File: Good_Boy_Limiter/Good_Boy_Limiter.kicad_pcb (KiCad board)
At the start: 2 copper layers, 36 parts, among them Q2 AO3422, SW3 RESET1, SW4 BOOT1, U1 ESP32-S3-WROOM-1, U2 TC4427EOA_C636891, U3 LM2576HVR-12, U4 LM2576SX-3.3/NOPB, U5 MAX40200AUK+T, U6 AMS1117-3.3, U7 MAX40200AUK+T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

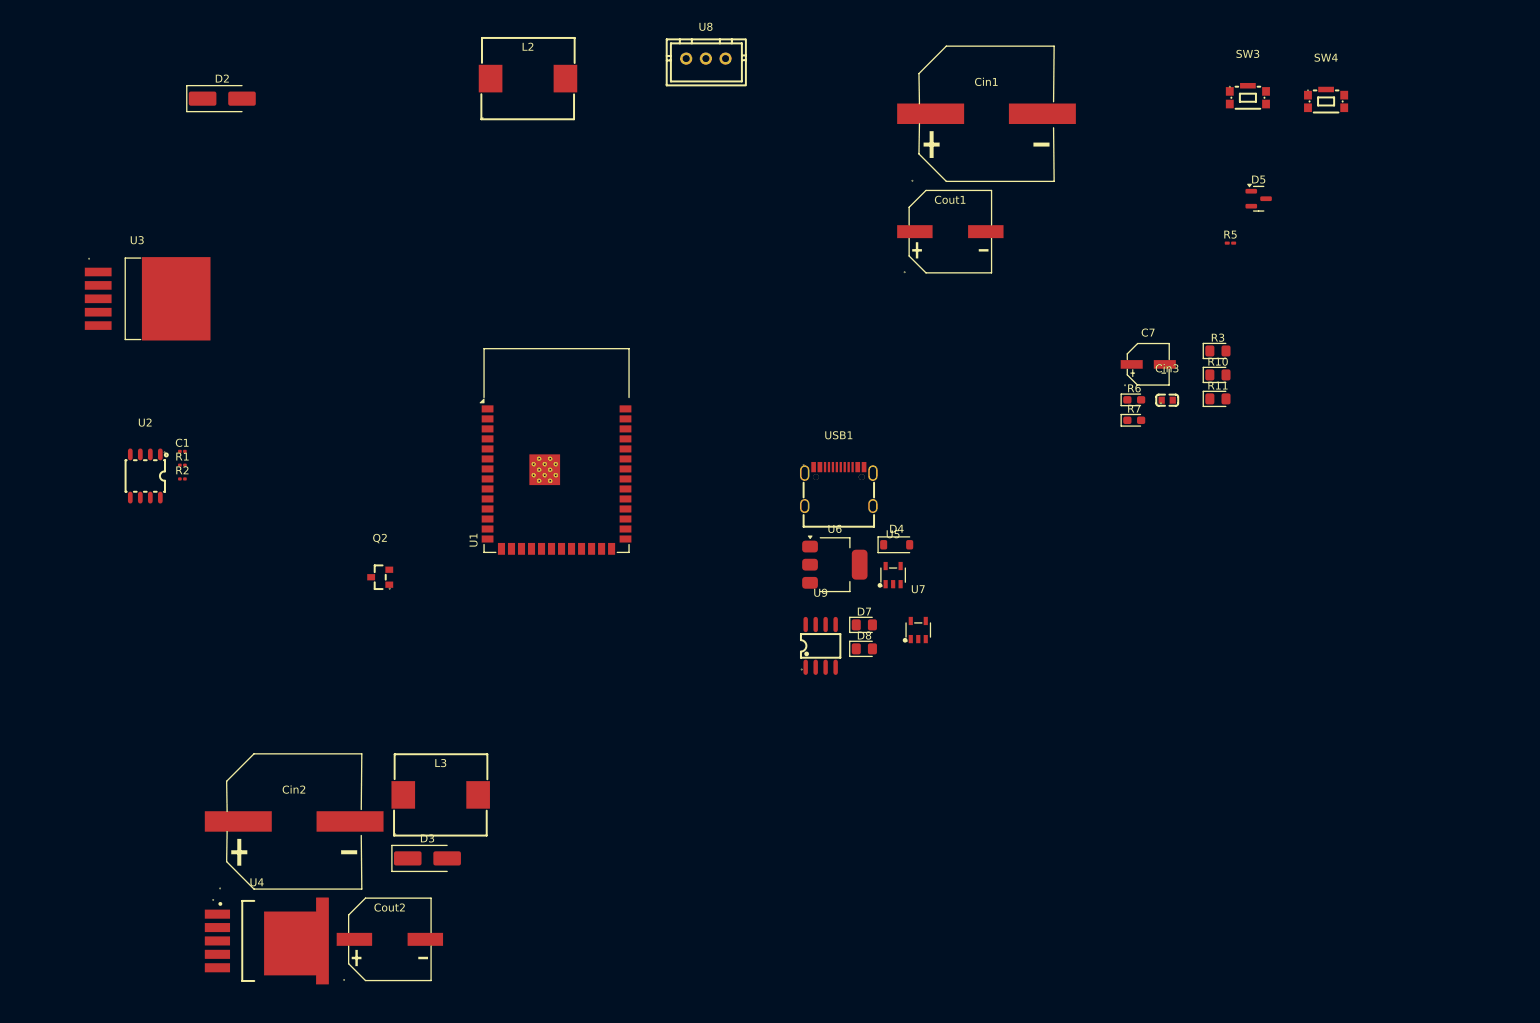
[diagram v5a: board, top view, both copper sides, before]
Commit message: Added all footprints
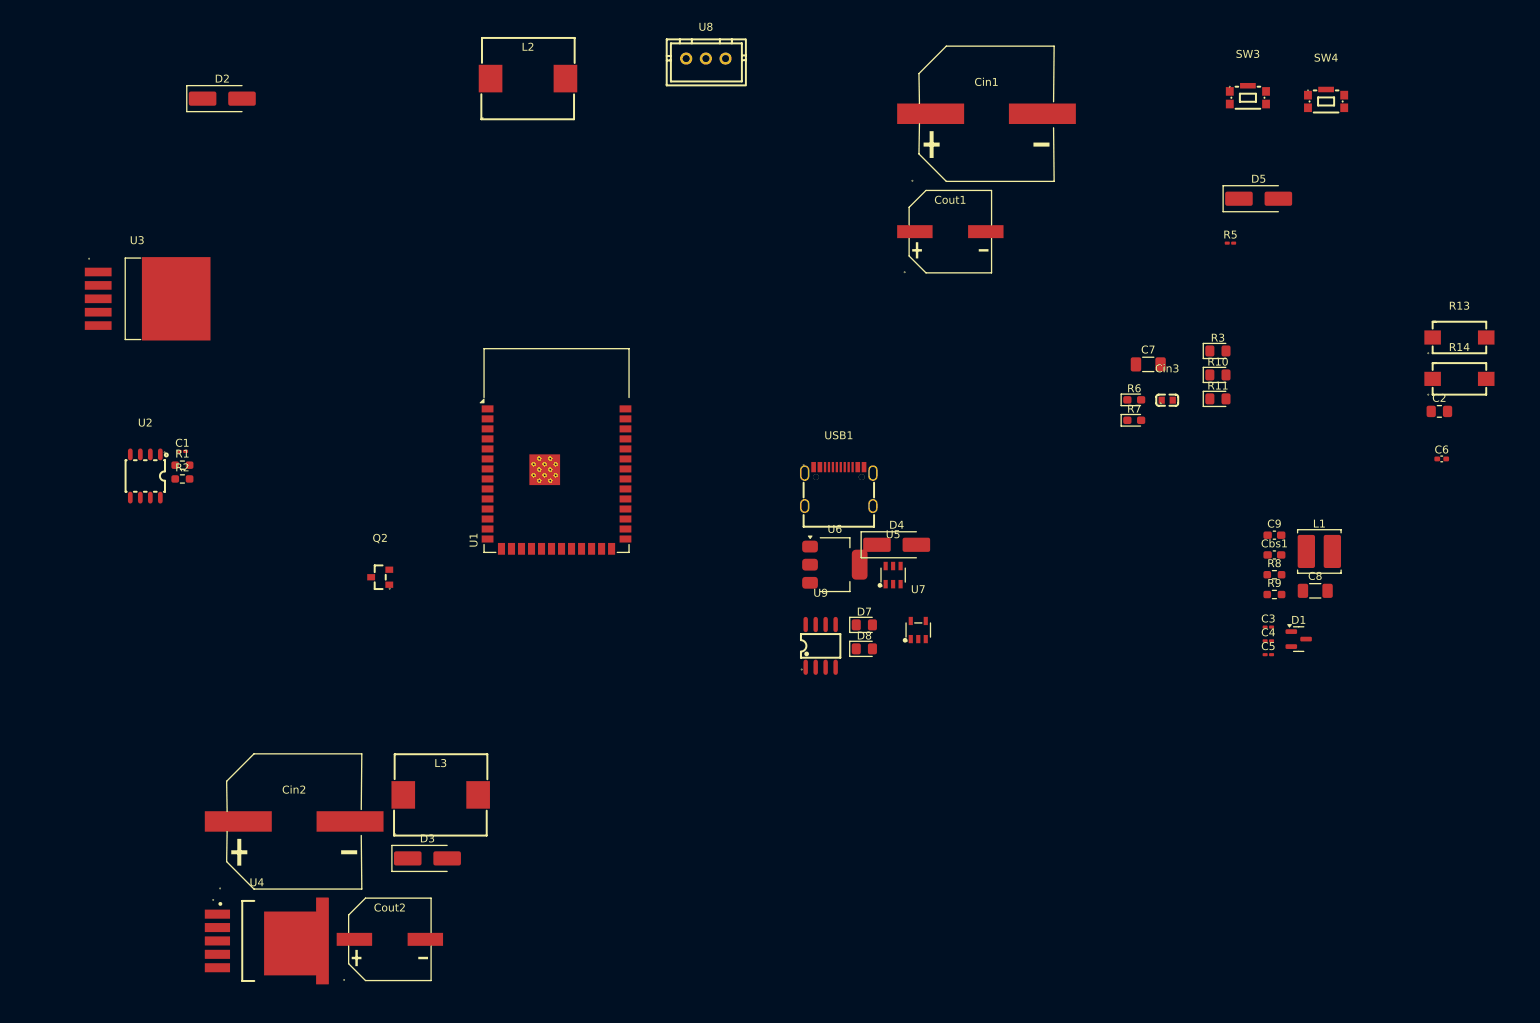
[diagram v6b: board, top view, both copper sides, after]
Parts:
- added C2: 1uF, Capacitor_SMD:C_0805_2012Metric_Pad1.18x1.45mm_HandSolder, F.Cu at (202.3, 70.2)
- added C3: 100nF, Capacitor_SMD:C_0201_0603Metric_Pad0.64x0.40mm_HandSolder, F.Cu at (180.6, 97.5)
- added C4: 10uF, Capacitor_SMD:C_0201_0603Metric_Pad0.64x0.40mm_HandSolder, F.Cu at (180.6, 99.3)
- added C5: 100nF, Capacitor_SMD:C_0201_0603Metric_Pad0.64x0.40mm_HandSolder, F.Cu at (180.6, 101.0)
- added C6: 100nF, Capacitor_SMD:C_0402_1005Metric_Pad0.74x0.62mm_HandSolder, F.Cu at (202.6, 76.2)
- added C8: 22uF, Capacitor_SMD:C_1206_3216Metric_Pad1.33x1.80mm_HandSolder, F.Cu at (186.6, 92.9)
- added C9: 100nF, Capacitor_SMD:C_0603_1608Metric_Pad1.08x0.95mm_HandSolder, F.Cu at (181.4, 85.9)
- added Cbs1: 10nF, Capacitor_SMD:C_0603_1608Metric_Pad1.08x0.95mm_HandSolder, F.Cu at (181.4, 88.4)
- added D1: 3V3, Package_TO_SOT_SMD:SOT-23, F.Cu at (184.5, 99.1)
- added L1: 10uH, Inductor_SMD:L_Cenker_CKCS5040, F.Cu at (187.1, 87.9)
- added R13: 100, easyeda2kicad:RES-SMD_L6.7-W4.0-LS7.9, F.Cu at (204.9, 60.8)
- added R14: 100, easyeda2kicad:RES-SMD_L6.7-W4.0-LS7.9, F.Cu at (204.9, 66.0)
- added R8: 100k, Resistor_SMD:R_0603_1608Metric_Pad0.98x0.95mm_HandSolder, F.Cu at (181.4, 90.9)
- added R9: 22k, Resistor_SMD:R_0603_1608Metric_Pad0.98x0.95mm_HandSolder, F.Cu at (181.4, 93.4)
- C1: footprint Capacitor_SMD:C_0201_0603Metric -> Capacitor_SMD:C_0201_0603Metric_Pad0.64x0.40mm_HandSolder
- C7: footprint easyeda2kicad:CAP-SMD_BD5.0-L5.3-W5.3-FD -> Capacitor_SMD:C_1206_3216Metric_Pad1.33x1.80mm_HandSolder
- D4: value 1N4148W -> SS34; footprint Diode_SMD:D_SOD-123 -> Diode_SMD:D_SMA_Handsoldering
- D5: value 3V3 -> SS34; footprint Package_TO_SOT_SMD:SOT-23 -> Diode_SMD:D_SMA_Handsoldering
- R1, R2: footprint Resistor_SMD:R_0201_0603Metric -> Resistor_SMD:R_0603_1608Metric_Pad0.98x0.95mm_HandSolder
- U5: value MAX40200AUK+T -> SY8120B; footprint easyeda2kicad:TSOT-23-5_L2.9-W1.6-P0.95-LS2.8-BL -> easyeda2kicad:SOT-23-6_L2.9-W1.6-P0.95-LS2.8-BL
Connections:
- C7 pad 1: Net-(C7-Pad1) -> /3V3
- D4 pad 1: /USB Communication/+5VUSB -> /3V3 Selector/Vin
- D4 pad 2: /3V3LDO -> /5VUSB
- D5 pad 1: GND -> /3V3 Selector/Vin
- D5 pad 2: unconnected-(D5-NC-Pad2) -> /+12V
- U5 pad 1: /3V3LDO -> Net-(U5-BS)
- U5 pad 3: /3V3LDO -> Net-(U5-FB)
- U5 pad 4: unconnected-(U5-N.C.-Pad4) -> /3V3 Selector/Vin
- U5 pad 5: /3V3 -> /3V3 Selector/Vin
- U9 pad 2: /3V3LDO -> /5VUSB
- U9 pad 3: /3V3Buck -> /+12V
- U9 pad 5: /3V3LDO -> /5VUSB
- U9 pad 6: /3V3Buck -> /+12V
- USB1 pad A4: /USB Communication/+5VUSB -> /5VUSB
- USB1 pad A9: /USB Communication/+5VUSB -> /5VUSB
- USB1 pad B4: /USB Communication/+5VUSB -> /5VUSB
- USB1 pad B9: /USB Communication/+5VUSB -> /5VUSB

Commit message: started some routing
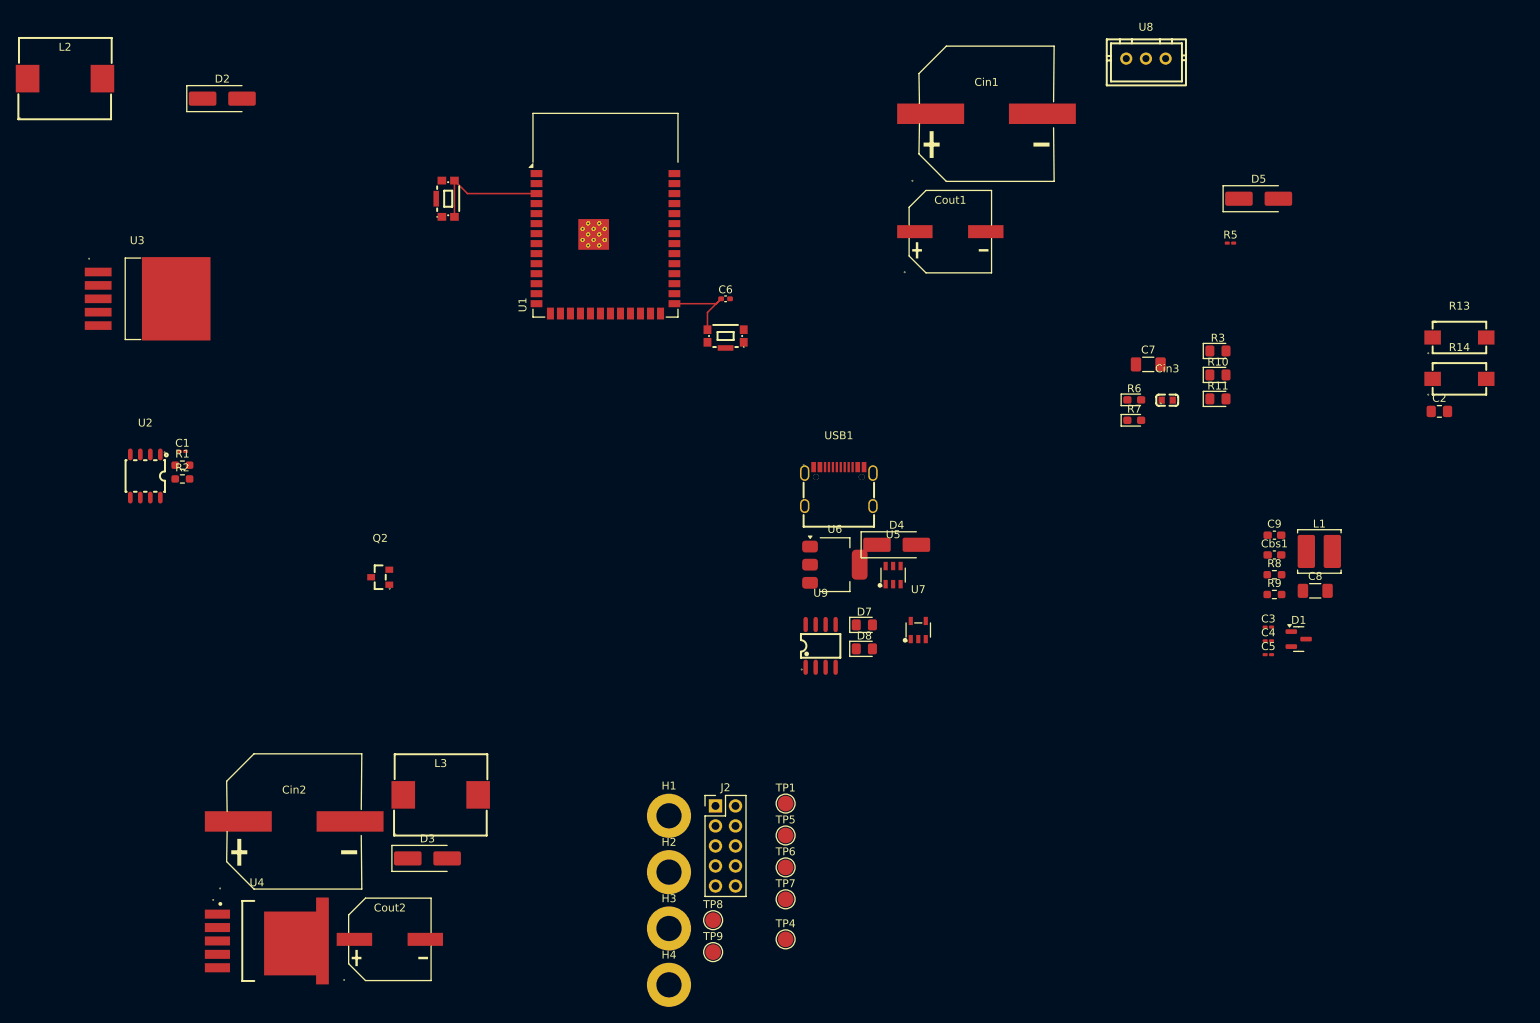
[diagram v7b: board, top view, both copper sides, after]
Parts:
- added H1: MountingHole_Pad, MountingHole:MountingHole_3.2mm_M3_DIN965_Pad, F.Cu at (104.6, 121.5)
- added H2: MountingHole_Pad, MountingHole:MountingHole_3.2mm_M3_DIN965_Pad, F.Cu at (104.6, 128.6)
- added H3: MountingHole_Pad, MountingHole:MountingHole_3.2mm_M3_DIN965_Pad, F.Cu at (104.6, 135.8)
- added H4: MountingHole_Pad, MountingHole:MountingHole_3.2mm_M3_DIN965_Pad, F.Cu at (104.6, 142.9)
- added J2: Extra General Pins, Connector_PinHeader_2.54mm:PinHeader_2x05_P2.54mm_Vertical, F.Cu at (110.5, 120.2)
- added TP1: 5VUSB, TestPoint:TestPoint_Pad_D2.0mm, F.Cu at (119.4, 119.9)
- added TP4: GND, TestPoint:TestPoint_Pad_D2.0mm, F.Cu at (119.4, 137.2)
- added TP5: 3V3, TestPoint:TestPoint_Pad_D2.0mm, F.Cu at (119.4, 124.0)
- added TP6: +12V, TestPoint:TestPoint_Pad_D2.0mm, F.Cu at (119.4, 128.0)
- added TP7: Vin, TestPoint:TestPoint_Pad_D2.0mm, F.Cu at (119.4, 132.1)
- added TP8: 48VOUT, TestPoint:TestPoint_Pad_D2.0mm, F.Cu at (110.2, 134.7)
- added TP9: 48VIN, TestPoint:TestPoint_Pad_D2.0mm, F.Cu at (110.2, 138.8)
- SW3: value RESET1 -> RESET
- SW4: value BOOT1 -> BOOT
- moved SW3 102.7 mm to (76.2, 43.2), turned to 90 degrees
- moved C6 93.1 mm to (111.8, 55.9)
- moved SW4 82.1 mm to (111.8, 61.0), turned to 180 degrees
- moved L2 58.8 mm to (27.9, 27.9)
- moved U8 55.8 mm to (165.1, 25.4)
- moved U1 30.5 mm to (96.5, 45.2)
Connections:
- U1 pad 12: unconnected-(U1-IO8-Pad12) -> /SDA
- U1 pad 17: unconnected-(U1-IO9-Pad17) -> /SCL
- U1 pad 36: unconnected-(U1-RXD0-Pad36) -> /RX
- U1 pad 37: unconnected-(U1-TXD0-Pad37) -> /TX
- U1 pad 4: unconnected-(U1-IO4-Pad4) -> /GPIO4
- U1 pad 5: unconnected-(U1-IO5-Pad5) -> /GPIO5
- U1 pad 8: unconnected-(U1-IO15-Pad8) -> /GPIO15
- U1 pad 9: unconnected-(U1-IO16-Pad9) -> /GPIO16
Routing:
- net Net-(U1-EN): track 0.00 -> 15.7 mm
- net /GPIO0: track 0.00 -> 10.8 mm

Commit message: fix: added 4 voltage sensing modules to measure all the 4 PDBs
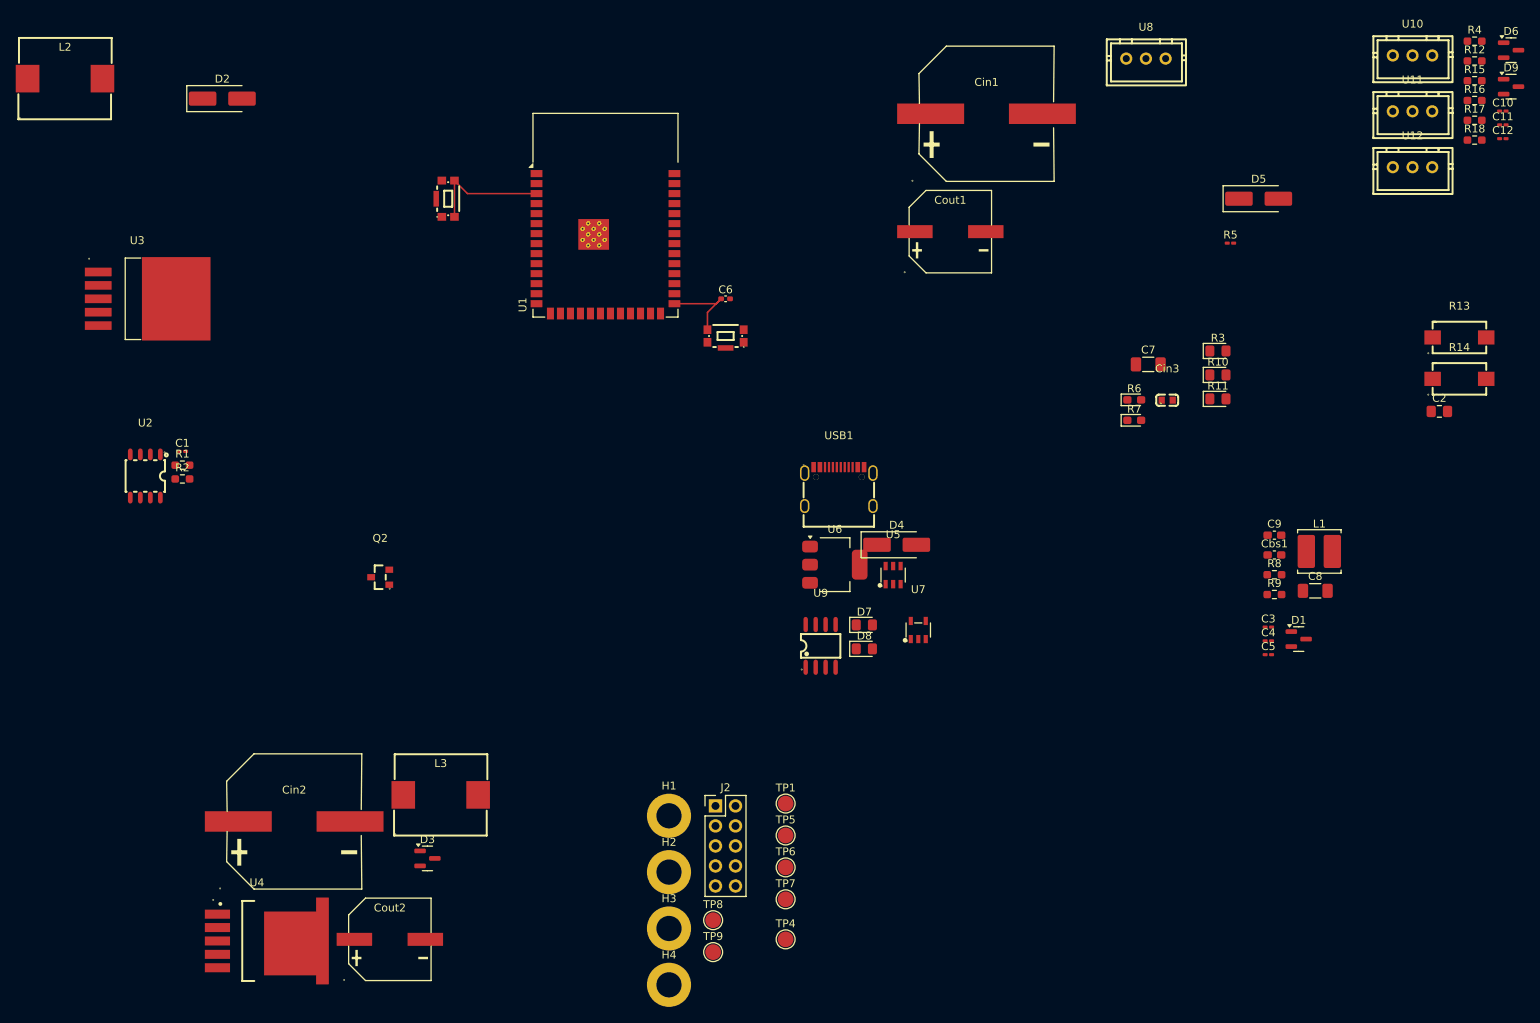
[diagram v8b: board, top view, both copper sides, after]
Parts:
- added C10: 100nF, Capacitor_SMD:C_0201_0603Metric_Pad0.64x0.40mm_HandSolder, F.Cu at (210.4, 32.1)
- added C11: 100nF, Capacitor_SMD:C_0201_0603Metric_Pad0.64x0.40mm_HandSolder, F.Cu at (210.4, 33.8)
- added C12: 100nF, Capacitor_SMD:C_0201_0603Metric_Pad0.64x0.40mm_HandSolder, F.Cu at (210.4, 35.6)
- added D6: 3V3, Package_TO_SOT_SMD:SOT-23, F.Cu at (211.4, 24.3)
- added D9: 3V3, Package_TO_SOT_SMD:SOT-23, F.Cu at (211.4, 29.0)
- added R12: 100k, Resistor_SMD:R_0603_1608Metric_Pad0.98x0.95mm_HandSolder, F.Cu at (206.8, 25.7)
- added R15: 4.7k, Resistor_SMD:R_0603_1608Metric_Pad0.98x0.95mm_HandSolder, F.Cu at (206.8, 28.2)
- added R16: 100k, Resistor_SMD:R_0603_1608Metric_Pad0.98x0.95mm_HandSolder, F.Cu at (206.8, 30.7)
- added R17: 4.7k, Resistor_SMD:R_0603_1608Metric_Pad0.98x0.95mm_HandSolder, F.Cu at (206.8, 33.2)
- added R18: 100k, Resistor_SMD:R_0603_1608Metric_Pad0.98x0.95mm_HandSolder, F.Cu at (206.8, 35.7)
- added R4: 4.7k, Resistor_SMD:R_0603_1608Metric_Pad0.98x0.95mm_HandSolder, F.Cu at (206.8, 23.2)
- added U10: B3B-XH-A, easyeda2kicad:CONN-TH_3P-P2.50_A2501WV2-3P, F.Cu at (198.9, 25.0)
- added U11: B3B-XH-A, easyeda2kicad:CONN-TH_3P-P2.50_A2501WV2-3P, F.Cu at (198.9, 32.1)
- added U12: B3B-XH-A, easyeda2kicad:CONN-TH_3P-P2.50_A2501WV2-3P, F.Cu at (198.9, 39.2)
- D3: value SS36 -> 3V3; footprint Diode_SMD:D_SMA_Handsoldering -> Package_TO_SOT_SMD:SOT-23
- SW3: value RESET -> RESET1
- SW4: value BOOT -> BOOT1
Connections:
- net /V_Sensing renamed /Voltage Sensing Modules/V_Sensing
- D3 pad 1: Net-(D3-K) -> GND
- D3 pad 2: GND -> unconnected-(D3-NC-Pad2)
- J2 pad 10: /GPIO4 -> /GPIO6
- J2 pad 9: /GPIO5 -> /GPIO7
- U1 pad 15: unconnected-(U1-IO3-Pad15) -> /GPIO3
- U1 pad 6: unconnected-(U1-IO6-Pad6) -> /GPIO6
- U1 pad 7: unconnected-(U1-IO7-Pad7) -> /GPIO7
- U2 pad 2: /GPIO2 -> /GPIO5
